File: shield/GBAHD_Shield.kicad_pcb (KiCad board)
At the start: 2 copper layers, 53.4 x 53.1 mm, 37 parts, among them J1 Conn_01x01, J10 Conn_01x10, J11 Conn_02x03_Odd_Even, J2 FFC_OGBA_32, J3 FFC_GBA-SP, J4 Conn_01x16, J5 FFC_OGBA_40, J6 Conn_01x06, J7 Conn_01x08, J8 Conn_01x10, J9 Conn_01x08, Q1 Q_PMOS_GSD, SW1 SW_Push, T1 Conn_01x01, T2 Conn_01x01, T3 Conn_01x01, T4 Conn_01x01, T5 Conn_01x01, T6 Conn_01x01, T7 Conn_01x01, T8 Conn_01x01, U1 AZ1117R-ADJ, U2 74HC595, U3 74HC595, U4 SNES_7PIN, U5 ATmega328P-AU

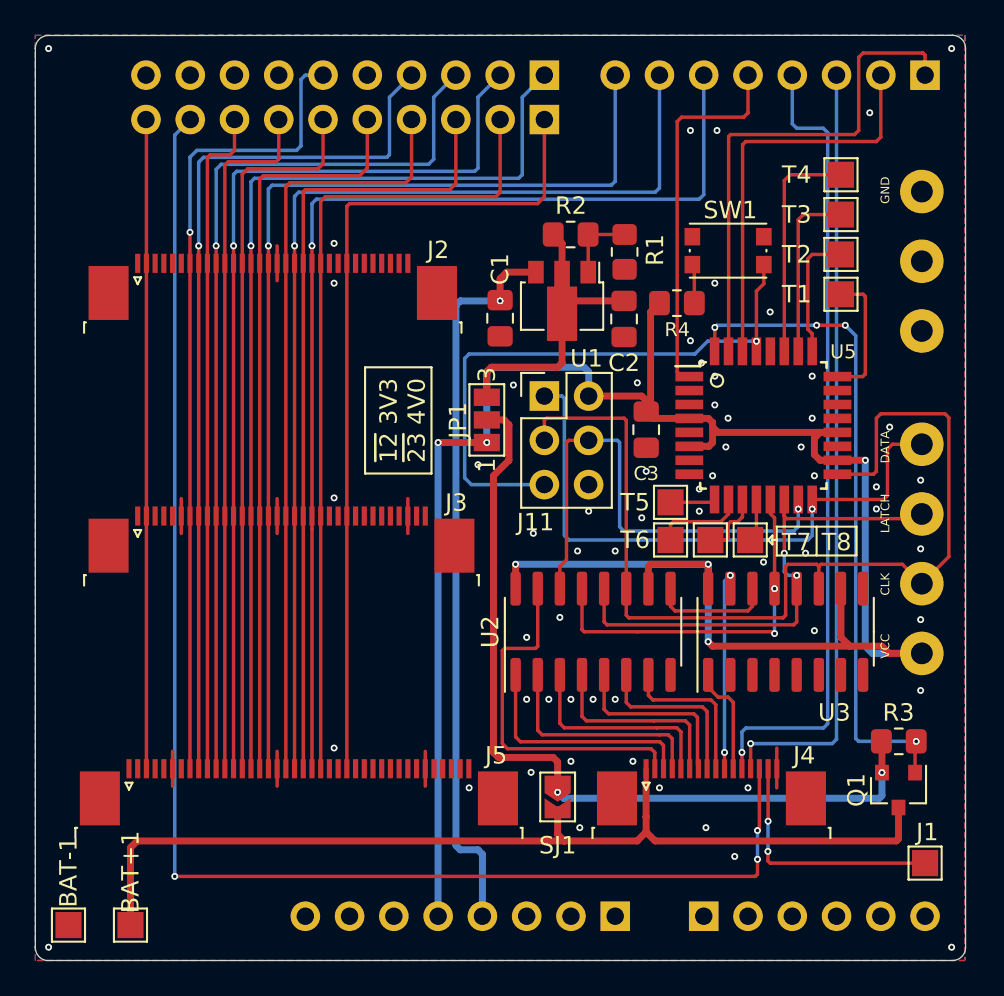
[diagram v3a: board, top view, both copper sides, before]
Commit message: some minor changes
* improved SP compatibility
* changed via diameter to 0.6mm and holesize to 0.3mm
* updated Readme
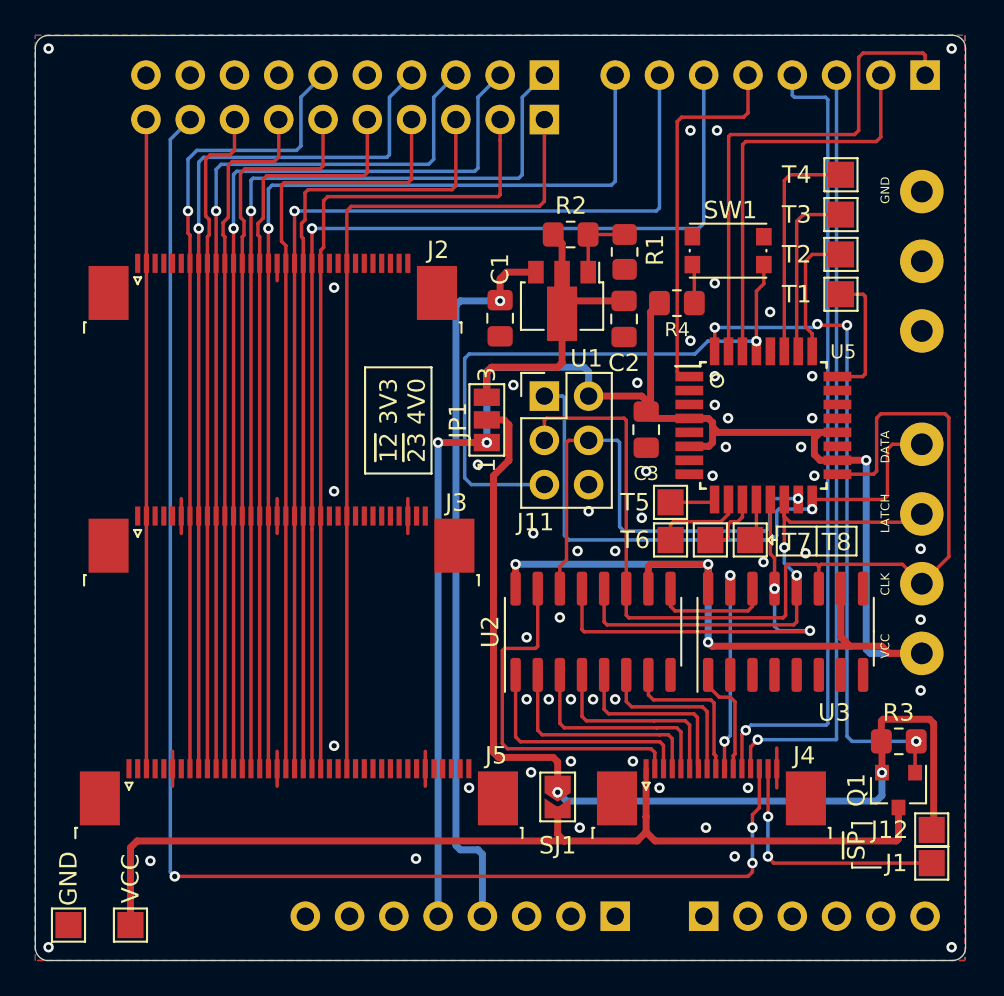
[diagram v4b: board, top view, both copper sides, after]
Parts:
- added J12: Conn_01x01, TestPoint:TestPoint_Pad_1.5x1.5mm, F.Cu at (91.1, 72.0)
- moved J1 0.38 mm to (91.1, 73.9)
- renumbered BAT-1 to GND, BAT+1 to VCC
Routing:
- net VCC: track 47.7 -> 57.9 mm
- net ~GBA_BUTTONS_EN~: track 21.3 -> 25.0 mm
- net GND: track 16.3 -> 15.3 mm, vias 60 -> 53
- net GB_R5: track 46.9 -> 46.4 mm
- net (no net): vias 1 -> 0
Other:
- net class Default: via_dia 0.4 -> 0.6; via_drill 0.2 -> 0.3
- net class VCC: via_dia 0.4 -> 0.6; via_drill 0.2 -> 0.3
- rule via_min_drill: 0.2 -> 0.3
- rule via_min_size: 0.4 -> 0.6
- board text added: "ManCloud 2021 Designed in Germany v20210416"
- board text added: "~SP~"
- board text removed: "ManCloud 2021 Designed in Germany v20210406"

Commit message: Develop (#16)
* Remove get_components from Makefile, fix bluepad path

* Fixed naming of submodule

* Fixed submodule mess

* Removed bluepad32

* Re-Add Bluepad32 properly

* Update Build for adding web/bitstream handler

* Add implementation for web handler and bitstream handler

* Update arduino version

* Fix build by using bluepad template as component foundation

* Removed bluepad submodule

* Copying default component files

* Remove get_components

* Improved over all build config

* Overall refactoring and added wifi and mega handler

* Minor updates to sdkconfig

* Add first crude version to update firmware

* Remove Bluepad Debug outputs

* some cleanup

* updated .gitignore and added some files

* updated gitmodules

* fixed submodules

* Update Upgrade function

* Fix gitignore

* Fix SPIFFS upload

* a little bit of tinkering

* Changed order of run/init to be faster for TWI

* Removed endTransmission after requestFrom

* changed twi handling

* added definition for bigger I2C-Buffer

* some cleanup

* remove wifi

* Fix sending of inputs without controller available

* Fix WiFi

* fixed button mapping

* fixed button mappings and polling intervalls

* Improve Timer Code

* Refactoring and Preferences

* Add Prefs

* Add prefs

* fixed verify_flash() --> missing beginTransmission()

* Added Bluetooth Mapping, Preferences Refactoring

* Add bluetooth cfg

* Refactoring

* Remove template

* CMake fixes

* changed TWI handling - added data validity timeout

* some cleanup

* Added License Hadder

* updated CPU-flex

* Refactoring

* Beautifying

* Update Bitstream

* refactored avr-firmware to be makefile project

* added controller detection

* Better layout

* Better shield handling

* Better OTA

* For now - only load bitstream from SPIFFS to be faster

* Add Force option for ATMega update

* Added Force Option for Mega Update

* Upd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
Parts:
- removed GND, J12, T8, VCC: Conn_01x01, TestPoint:TestPoint_Pad_1.5x1.5mm
- removed SJ1: SOLDER_JUMPER, Jumper:SolderJumper-2_P1.3mm_Open_TrianglePad1.0x1.5mm
- added C4: 47uF, Capacitor_SMD:C_0805_2012Metric_Pad1.18x1.45mm_HandSolder, B.Cu at (74.9, 51.0)
- added D1: RED, LED_SMD:LED_0805_2012Metric_Pad1.15x1.40mm_HandSolder, B.Cu at (75.8, 48.4)
- added D2: GREEN, LED_SMD:LED_0805_2012Metric_Pad1.15x1.40mm_HandSolder, B.Cu at (75.8, 42.3)
- added GND1: Conn_01x01, TestPoint:TestPoint_Pad_1.5x1.5mm, F.Cu at (46.2, 77.0)
- added Q2: Q_NMOS_GSD, Package_TO_SOT_SMD:SOT-23, B.Cu at (74.9, 59.4)
- added Q3: Q_NMOS_GSD, Package_TO_SOT_SMD:SOT-23, B.Cu at (70.0, 62.0)
- added R5: 500, Resistor_SMD:R_0805_2012Metric_Pad1.20x1.40mm_HandSolder, B.Cu at (77.7, 56.9)
- added R6: 1k, Resistor_SMD:R_0805_2012Metric_Pad1.20x1.40mm_HandSolder, B.Cu at (75.8, 46.4)
- added R7: 1k, Resistor_SMD:R_0805_2012Metric_Pad1.20x1.40mm_HandSolder, B.Cu at (75.8, 44.3)
- added R8: 10K, Resistor_SMD:R_0805_2012Metric_Pad1.20x1.40mm_HandSolder, B.Cu at (72.1, 56.9)
- added VCC1: Conn_01x01, TestPoint:TestPoint_Pad_1.5x1.5mm, F.Cu at (50.0, 77.0)
- C1, C2, C3, Q1, R1, R2, R3, R4, U2, U3: moved to B.Cu
- T1, T2, T5: footprint TestPoint:TestPoint_Pad_1.5x1.5mm -> TestPoint:TestPoint_Pad_D1.5mm
- T3, T4, T6, T7: footprint TestPoint:TestPoint_Pad_1.5x1.5mm -> TestPoint:TestPoint_Pad_D1.5mm; moved to B.Cu
- moved R2 25.1 mm to (81.9, 60.1), turned to 0 degrees
- moved C1 23.5 mm to (84.8, 57.1), turned to -90 degrees
- moved U1 21.0 mm to (82.9, 58.0), turned to 90 degrees
- moved R3 19.9 mm to (74.9, 53.1), turned to 0 degrees
- moved Q1 19.8 mm to (74.9, 55.9)
- moved R1 19.7 mm to (80.8, 57.1), turned to -90 degrees
- moved T4 18.9 mm to (68.3, 41.4)
- moved C2 17.2 mm to (82.8, 57.1), turned to -90 degrees
- moved T3 15.5 mm to (70.7, 40.0)
- moved T7 15.4 mm to (79.2, 40.0)
- moved J11 15.0 mm to (82.8, 41.5)
- moved JP1 14.9 mm to (75.1, 59.9), turned to 0 degrees
- moved T2 14.6 mm to (71.2, 38.1)
- moved SW1 13.4 mm to (84.2, 51.3), turned to 0 degrees
- moved T1 12.4 mm to (73.9, 38.1)
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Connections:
- net PIXEL_GRID renamed FPGA_COM
- net ~GBA_BUTTONS_EN~ renamed ~{GBA_BUTTONS_EN}
- J10 pad 10: (no net) -> SP_ARSCL
- J10 pad 5: (no net) -> SP_ARD12
- J10 pad 8: (no net) -> unconnected-(J10-Pad8)
- J10 pad 9: (no net) -> SP_ARSDA
- J2 pad 1: (no net) -> unconnected-(J2-Pad1)
- J2 pad 23: (no net) -> unconnected-(J2-Pad23)
- J2 pad 24: (no net) -> unconnected-(J2-Pad24)
- J2 pad 26: (no net) -> unconnected-(J2-Pad26)
- J2 pad 27: (no net) -> unconnected-(J2-Pad27)
- J2 pad 28: (no net) -> unconnected-(J2-Pad28)
- J2 pad 29: (no net) -> unconnected-(J2-Pad29)
- J2 pad 3: (no net) -> unconnected-(J2-Pad3)
- J2 pad 30: (no net) -> unconnected-(J2-Pad30)
- J2 pad 31: (no net) -> unconnected-(J2-Pad31)
- J2 pad 32: (no net) -> unconnected-(J2-Pad32)
- J2 pad 4: (no net) -> unconnected-(J2-Pad4)
- J2 pad 5: (no net) -> unconnected-(J2-Pad5)
- J2 pad 6: (no net) -> unconnected-(J2-Pad6)
- J3 pad 1: (no net) -> unconnected-(J3-Pad1)
- J3 pad 23: (no net) -> unconnected-(J3-Pad23)
- J3 pad 24: (no net) -> unconnected-(J3-Pad24)
- J3 pad 26: (no net) -> unconnected-(J3-Pad26)
- J3 pad 27: (no net) -> unconnected-(J3-Pad27)
- J3 pad 28: (no net) -> unconnected-(J3-Pad28)
- J3 pad 29: (no net) -> unconnected-(J3-Pad29)
- J3 pad 3: (no net) -> unconnected-(J3-Pad3)
- J3 pad 30: (no net) -> unconnected-(J3-Pad30)
- J3 pad 31: (no net) -> unconnected-(J3-Pad31)
- J3 pad 33: (no net) -> unconnected-(J3-Pad33)
- J3 pad 34: (no net) -> unconnected-(J3-Pad34)
- J3 pad 4: (no net) -> unconnected-(J3-Pad4)
- J3 pad 5: (no net) -> unconnected-(J3-Pad5)
- J4 pad 14: GBA_CLK -> GBA_CLK'
- J5 pad 1: (no net) -> unconnected-(J5-Pad1)
- J5 pad 2: (no net) -> unconnected-(J5-Pad2)
- J5 pad 24: (no net) -> unconnected-(J5-Pad24)
- J5 pad 25: (no net) -> unconnected-(J5-Pad25)
- J5 pad 27: (no net) -> unconnected-(J5-Pad27)
- J5 pad 28: (no net) -> unconnected-(J5-Pad28)
- J5 pad 29: (no net) -> unconnected-(J5-Pad29)
- J5 pad 30: (no net) -> unconnected-(J5-Pad30)
- J5 pad 31: (no net) -> unconnected-(J5-Pad31)
- J5 pad 32: (no net) -> unconnected-(J5-Pad32)
- J5 pad 33: (no net) -> unconnected-(J5-Pad33)
- J5 pad 34: (no net) -> unconnected-(J5-Pad34)
- J5 pad 36: (no net) -> unconnected-(J5-Pad36)
- J5 pad 37: (no net) -> unconnected-(J5-Pad37)
- J5 pad 38: (no net) -> unconnected-(J5-Pad38)
- J5 pad 39: (no net) -> unconnected-(J5-Pad39)
- J5 pad 4: (no net) -> unconnected-(J5-Pad4)
- J5 pad 40: (no net) -> unconnected-(J5-Pad40)
- J5 pad 5: (no net) -> unconnected-(J5-Pad5)
- J5 pad 7: (no net) -> unconnected-(J5-Pad7)
- J6 pad 1: (no net) -> AR_A0
- J6 pad 2: (no net) -> AR_A1
- J6 pad 3: (no net) -> AR_A2
- J6 pad 4: (no net) -> AR_A3
- J6 pad 5: (no net) -> AR_A4
- J6 pad 6: (no net) -> AR_A5
- J7 pad 1: (no net) -> SP_VIN
- J7 pad 6: (no net) -> SP_ARRES
- J7 pad 7: (no net) -> unconnected-(J7-Pad7)
- J7 pad 8: (no net) -> unconnected-(J7-Pad8)
- U3 pad 2: (no net) -> unconnected-(U3-Pad2)
- U3 pad 3: (no net) -> unconnected-(U3-Pad3)
- U3 pad 4: (no net) -> unconnected-(U3-Pad4)
- U3 pad 5: (no net) -> unconnected-(U3-Pad5)
- U3 pad 6: (no net) -> unconnected-(U3-Pad6)
- U3 pad 7: (no net) -> unconnected-(U3-Pad7)
- U3 pad 9: (no net) -> unconnected-(U3-Pad9)
- U5 pad 10: Net-(T6-Pad1) -> LED_RED
- U5 pad 11: Net-(T7-Pad1) -> LED_GREEN
- U5 pad 12: Net-(T8-Pad1) -> Net-(T7-Pad1)
- U5 pad 19: (no net) -> unconnected-(U5-Pad19)
- U5 pad 2: (no net) -> Net-(T5-Pad1)
- U5 pad 22: (no net) -> unconnected-(U5-Pad22)
- U5 pad 23: (no net) -> Net-(T1-Pad1)
- U5 pad 24: Net-(T1-Pad1) -> Net-(T2-Pad1)
- U5 pad 25: Net-(T2-Pad1) -> Net-(T3-Pad1)
- U5 pad 26: Net-(T3-Pad1) -> Net-(T4-Pad1)
- U5 pad 27: Net-(T4-Pad1) -> SP_ARSDA
- U5 pad 28: (no net) -> SP_ARSCL
- U5 pad 7: (no net) -> unconnected-(U5-Pad7)
- U5 pad 8: (no net) -> unconnected-(U5-Pad8)
- U5 pad 9: Net-(T5-Pad1) -> Net-(T6-Pad1)
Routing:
- net VCC: track 57.9 -> 9.35 mm, vias 2 -> 1
- net SP_ARSCL: track 0.00 -> 41.9 mm, vias 0 -> 3
- net ICSP_MOSI: track 28.6 -> 67.9 mm, vias 1 -> 2
- net SP_ARSDA: track 0.00 -> 35.8 mm, vias 0 -> 1
- net SNS_LATCH: track 29.7 -> 63.4 mm, vias 2 -> 1
- net GBA_CLK: track 83.3 -> 52.7 mm, vias 3 -> 0
- net GBA_POWER_SEL: track 38.6 -> 14.1 mm, vias 4 -> 1
- net GBA_CLK': track 0.00 -> 18.0 mm, vias 0 -> 1
- net ~{GBA_BUTTONS_EN}: track 25.0 -> 42.7 mm, vias 2 -> 1
- net SP_ARD1: track 23.6 -> 37.6 mm, vias 0 -> 1
- net GBA_UP: track 20.7 -> 7.95 mm, vias 0 -> 1
- net RX: track 29.3 -> 41.9 mm, vias 0 -> 1
- net AT_RST: track 36.1 -> 25.0 mm
- net Net-(T4-Pad1): track 13.2 -> 2.88 mm, vias 0 -> 1
- net ICSP_MISO: track 34.1 -> 24.5 mm, vias 1 -> 0
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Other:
- board size 53.4 x 53.1 mm -> 48.3 x 51.8 mm
- net class Default removed
- net class VCC removed
- board text added: "ManCloud 2022 Designed in Germany v20220310"
- board text added: "~{12} 3V3 ~{23} 4V0"
- board text removed: "ManCloud 2021 Designed in Germany v20210416"
- board text removed: "~12~ 3V3 ~23~ 4V0"
- board text removed: "~SP~"
